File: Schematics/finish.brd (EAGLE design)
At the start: 100 x 80 mm, 9 parts, among them U1 TINY85-20-DIP

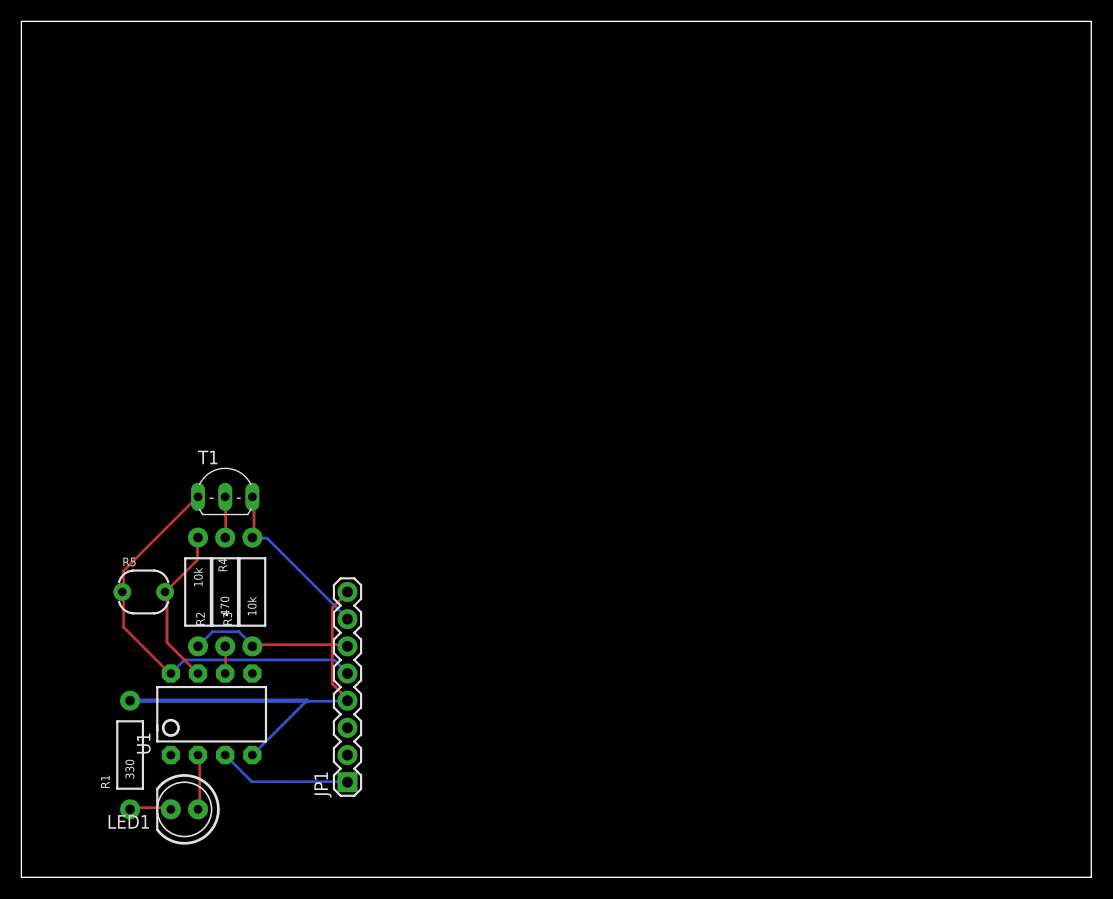
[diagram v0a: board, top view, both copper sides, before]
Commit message: routed finish sensor
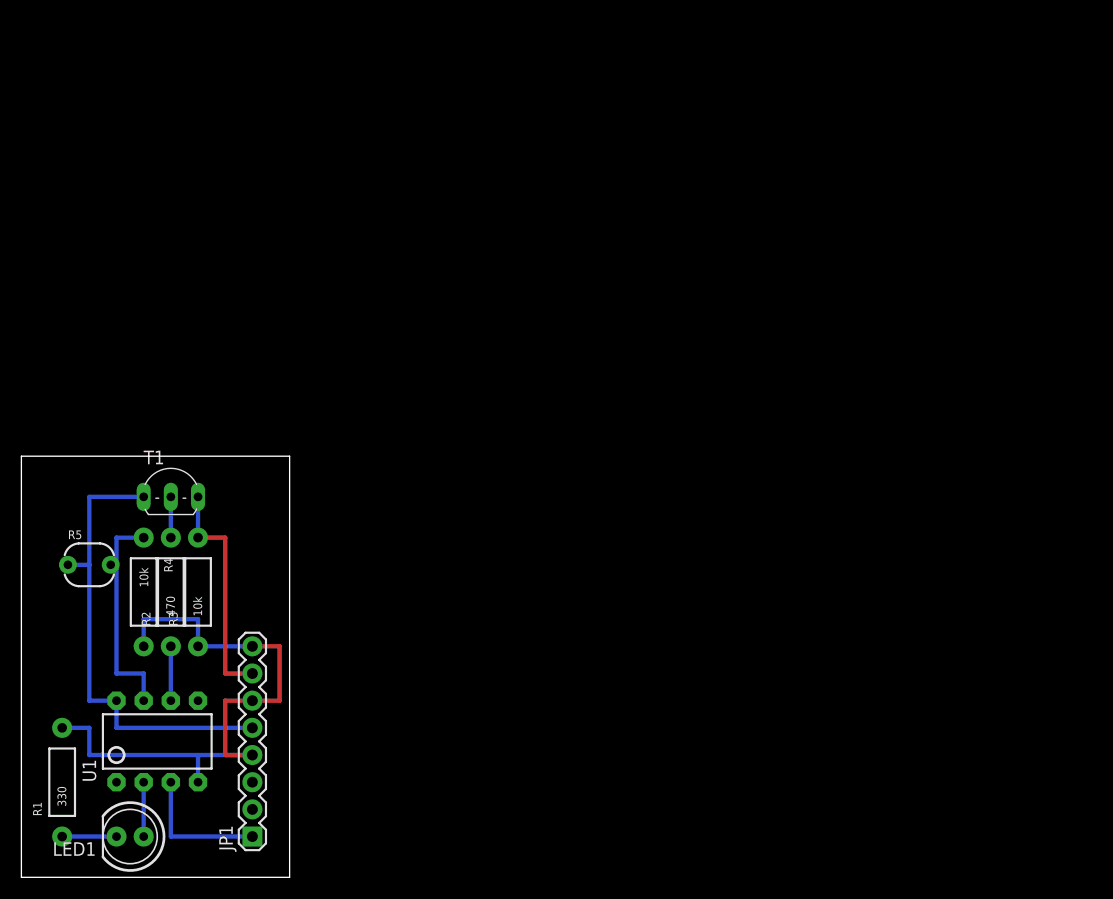
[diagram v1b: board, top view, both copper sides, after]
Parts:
- moved JP1 10.2 mm to (21.6, 3.81)
- moved R1 6.84 mm to (3.81, 8.89)
- moved U1 5.68 mm to (12.7, 12.7)
- moved LED1 5.68 mm to (10.2, 3.81)
- moved R5 5.68 mm to (6.35, 29.2)
- moved R4 5.08 mm to (11.4, 26.7)
- moved R2 5.08 mm to (14.0, 26.7)
- moved T1 5.08 mm to (14.0, 36.8)
- moved R3 5.08 mm to (16.5, 26.7)
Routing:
- net SENSE: track 15.3 -> 20.9 mm
- net SIGOUT: track 16.1 -> 21.6 mm
- net 5V: track 39.0 -> 43.9 mm
- net GND: track 54.4 -> 58.4 mm
- net SIGIN: track 2.58 -> 5.08 mm
- net N$1: track 4.03 -> 5.08 mm
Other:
- board size 100 x 80 mm -> 25.1 x 39.4 mm
